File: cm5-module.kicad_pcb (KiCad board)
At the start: 4 copper layers, 100 x 100 mm, 242 parts, among them J1 DIN-41612-connector_090319679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, J10 MicroSD_5033981892, J11 JST_SH_1x4_BM04B-SRSS-TB-LF-SN, J12 USB-C_USB-310F-B-SU, J2 CM5_1-100_3mm-stack, J3 CM5_101-200_3mm-stack, J4 JST_SH_1x3_BM03B-SRSS-TB-LF-SN, J5 Bus_M.2_1-2199230-6, J6 RJ45_HC612601A-M893-A, J7 USB-A_USB-303WSD-BRY, J8 HDMI-A_HDMI-19PIN-043, J9 USB-C_USB-310F-B-SU, Q1 SIS472DN-T1-GE3, Q10 AO3400A, Q2 SIS472DN-T1-GE3, Q3 AO3400A, Q4 SIS472DN-T1-GE3, Q5 AO3400A, Q6 AO3400A, Q7 AO3400A, Q8 AO3401A, Q9 AO3401A, SW1 SW_TL2243, U1 AP22615AWU-7, U10 AP22615AWU-7, U11 AP22615AWU-7, U12 LM74700QDBVRQ1, U13 STM32G431CBU6, U14 STM32G431CBU6, U15 TJA1044GTK_3Z, U16 TJA1044GTK_3Z, U17 FSUSB42UMX, U2 AP22615AWU-7, U3 FT230XQ-R, U4 NTS0102DP, U5 CH334P, U6 LM74700QDBVRQ1, U7 SIC431AED-T1-GE3, U8 LM74700QDBVRQ1, U9 TPS564247DRLR, Y1 Oscillator_32.768kHz_OK2EL89C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, Y2 X322512MSB4SI

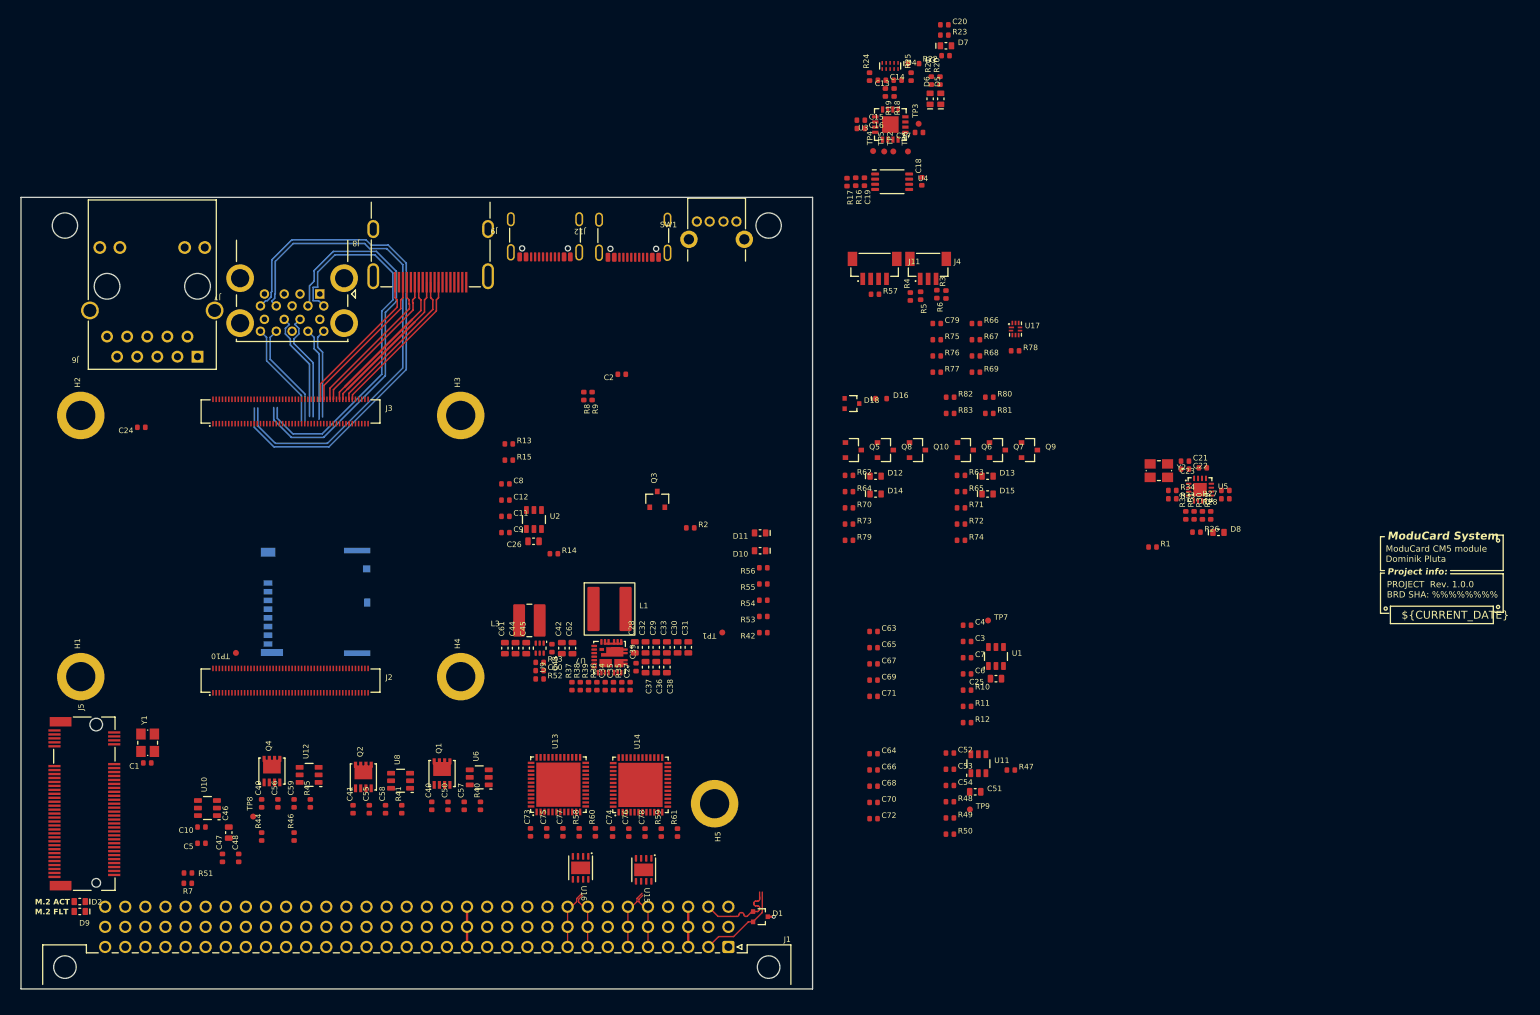
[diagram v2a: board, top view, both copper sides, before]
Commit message: [#3] Fix 3V3 DC-DC converter schematic, change one USB-C to a vertical one, start layout
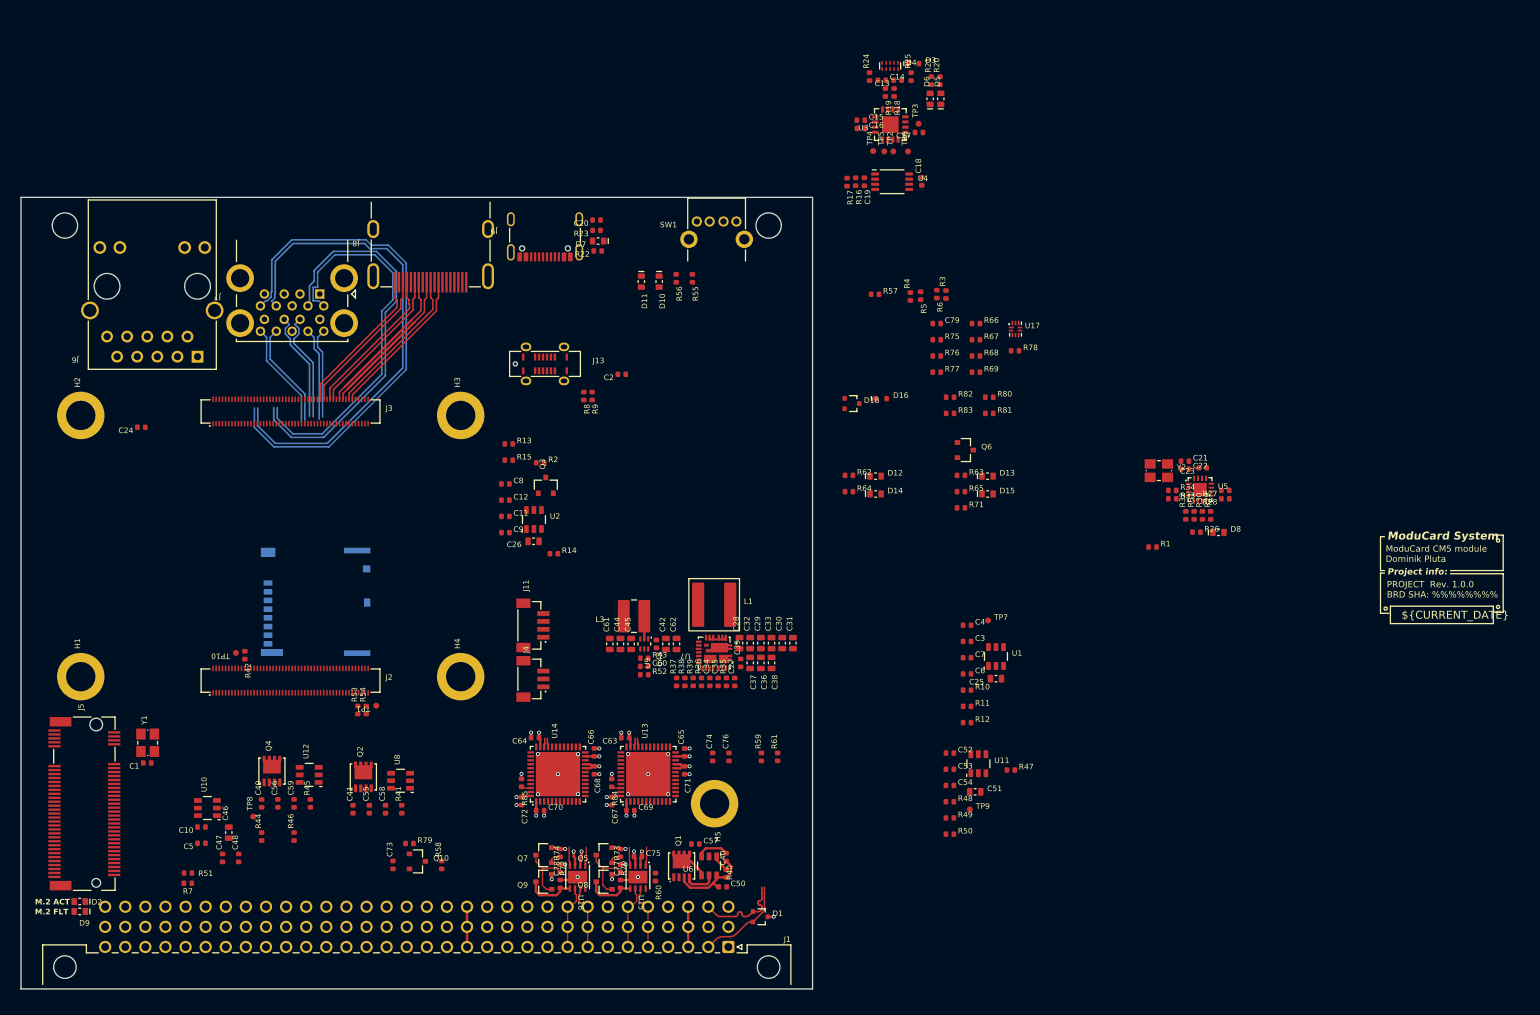
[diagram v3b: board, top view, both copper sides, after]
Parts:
- removed J12: USB-C_USB-310F-B-SU, DW-footprints:USB-C-Receptacle_USB-310-B-SU
- added J13: USB-C_TYPE-C_16PLT-H6.5, DW-footprints:USB-C-Receptacle_TYPE-C_16PLT-H6.5, F.Cu at (106.2, 71.0)
- added R84: R-10k-0402, DW-footprints:R_0402_1005Metric, F.Cu at (114.6, 124.0)
- added R85: R-10k-0402, DW-footprints:R_0402_1005Metric, F.Cu at (103.2, 124.0)
- moved Q9 82.1 mm to (106.0, 136.5), turned to 180 degrees
- moved Q10 81.8 mm to (90.1, 133.9)
- moved Q7 76.8 mm to (106.0, 133.1), turned to 180 degrees
- moved J4 72.6 mm to (104.2, 110.8), turned to 90 degrees
- moved R79 67.5 mm to (89.1, 131.6)
- moved R42 65.6 mm to (68.3, 107.8), turned to -90 degrees
- moved R72 65.5 mm to (108.1, 132.8), turned to -90 degrees
- moved R74 65.4 mm to (108.1, 134.8), turned to 90 degrees
- moved Q8 65.1 mm to (113.7, 136.5), turned to 180 degrees
- moved J11 63.1 mm to (104.2, 104.1), turned to 90 degrees
- moved Q5 60.1 mm to (113.7, 133.1), turned to 180 degrees
- moved R53 52.6 mm to (82.5, 114.8), turned to 90 degrees
- moved R70 52.3 mm to (115.7, 132.8), turned to -90 degrees
- moved R73 52.2 mm to (115.7, 134.8), turned to 90 degrees
- moved R54 52.1 mm to (83.6, 114.8), turned to 90 degrees
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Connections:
- net Net-(U9-FB) renamed /Power/3V3_FB
- C60 pad 2: Net-(U9-SW) -> +3V3
- L3 pad 1: Net-(U9-SW) -> /Power/3V3_SW
- R52 pad 2: Net-(U9-SW) -> +3V3
- U9 pad 2: Net-(U9-SW) -> /Power/3V3_SW
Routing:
- net +3V3: track 0.00 -> 22.9 mm, vias 0 -> 14
- net GND: track 0.76 -> 20.4 mm, vias 1 -> 29
- net +5V_STDBY: track 5.08 -> 15.8 mm
- net Net-(Q7-D): track 0.00 -> 7.97 mm
- net Net-(Q5-D): track 0.00 -> 7.97 mm
- net +5V: track 0.00 -> 7.21 mm, vias 0 -> 2
- net /CAN to USB 2/VIO: track 0.00 -> 6.42 mm
- net /CAN to USB 1/VIO: track 0.00 -> 6.42 mm
- net Net-(Q1-G): track 0.00 -> 4.14 mm
- net /Power/Ideal diode 0/~{DISABLE}: track 0.00 -> 4.08 mm
- net /CAN to USB 1/RXD: track 0.00 -> 3.60 mm
- net /CAN to USB 2/RXD: track 0.00 -> 3.60 mm
- net /Power/3V3_SW: track 0.00 -> 2.86 mm
- net /CAN to USB 2/TXD: track 0.00 -> 2.38 mm
- net /CAN to USB 1/TXD: track 0.00 -> 2.38 mm
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
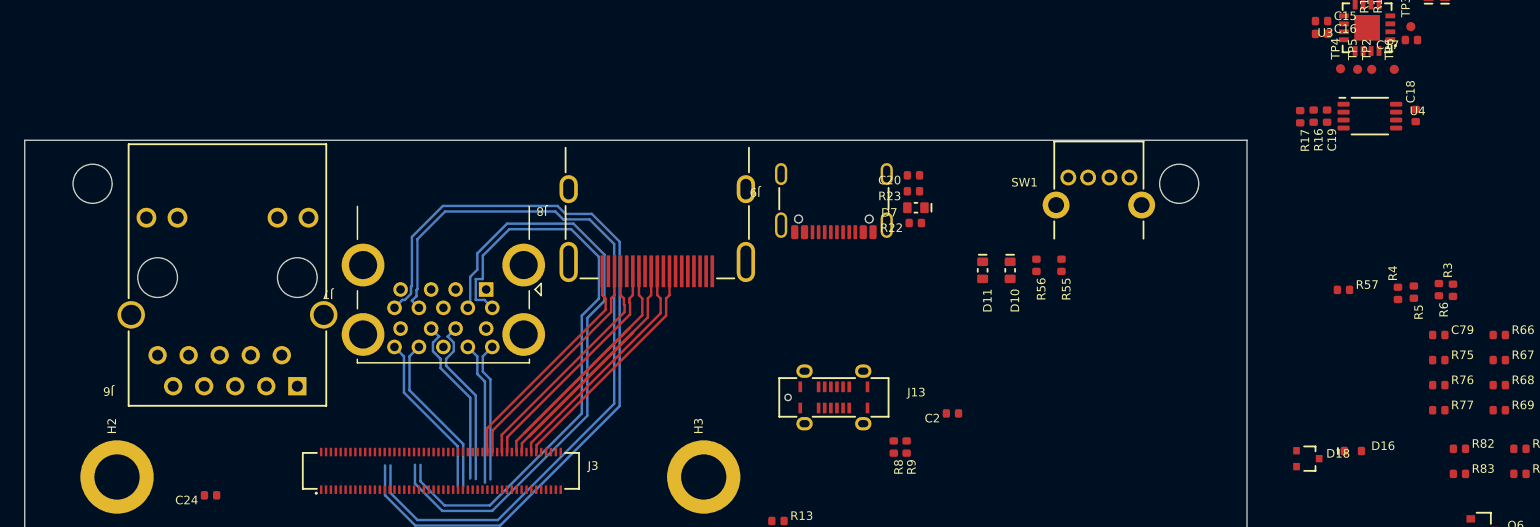
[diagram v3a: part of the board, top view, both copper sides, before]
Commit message: [#3] Adjust front panel mounting holes positioning and rails keepout area
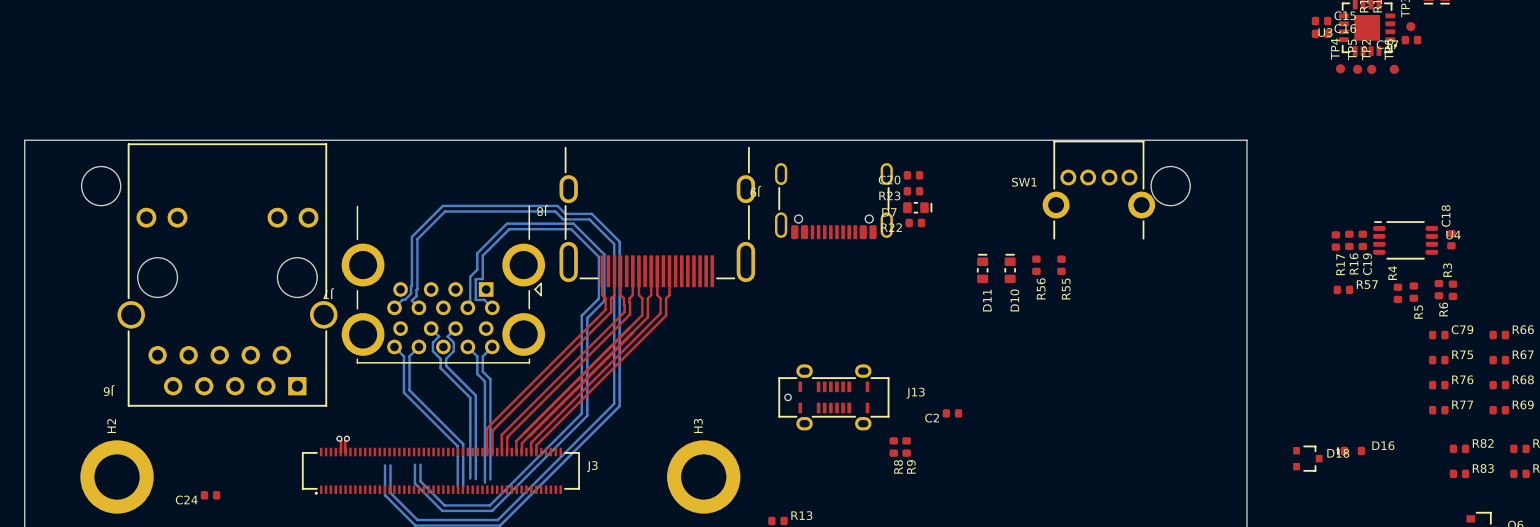
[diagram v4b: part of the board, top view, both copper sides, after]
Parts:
- moved R16 10.6 mm to (148.4, 58.2)
- moved R17 10.6 mm to (147.3, 58.2)
- moved C18 10.6 mm to (156.7, 58.1)
- moved C19 10.6 mm to (149.5, 58.2)
- moved U4 10.6 mm to (153.0, 58.2)
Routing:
- net /CM5/PCIe.REFCLK+: track 0.00 -> 1.16 mm, vias 0 -> 1
- net /CM5/PCIe.REFCLK-: track 0.00 -> 1.16 mm, vias 0 -> 1
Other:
- outline, holes or cut-outs redrawn

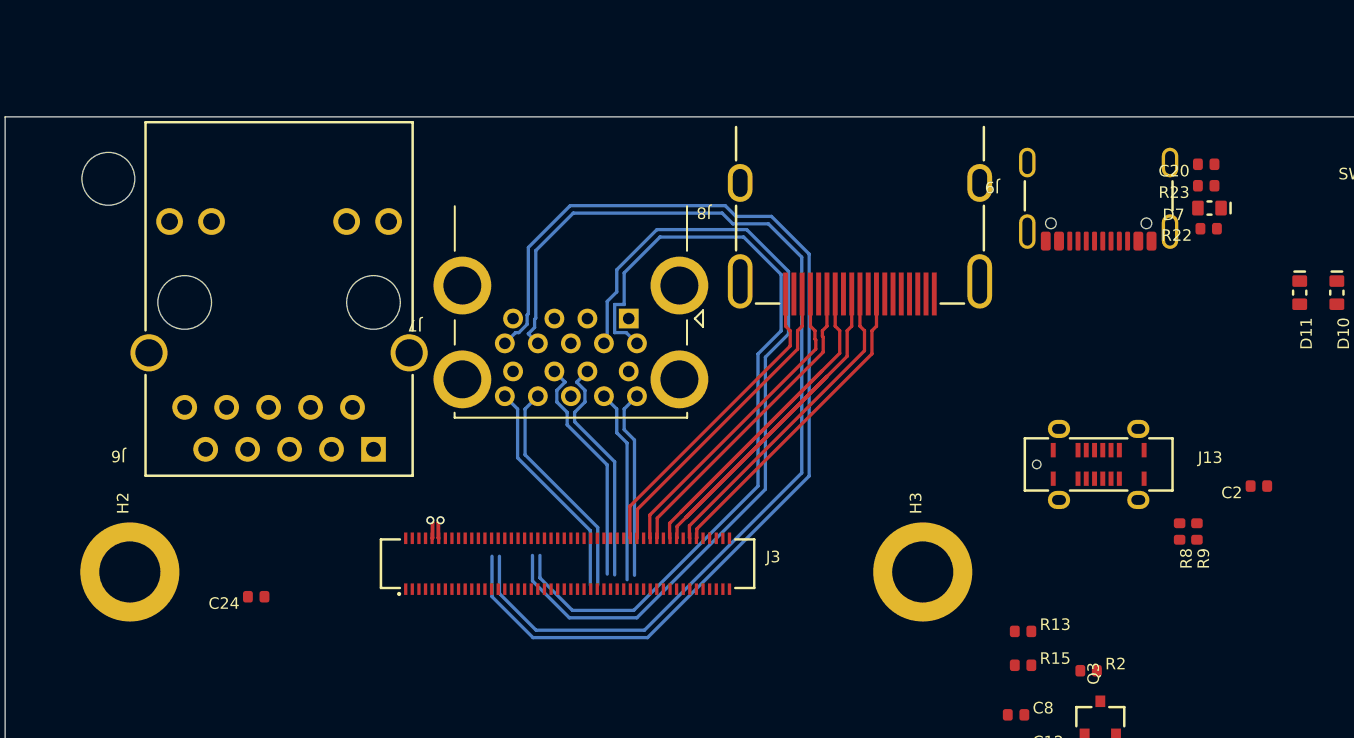
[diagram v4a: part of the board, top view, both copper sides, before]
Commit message: [#3] Position front panel connectors
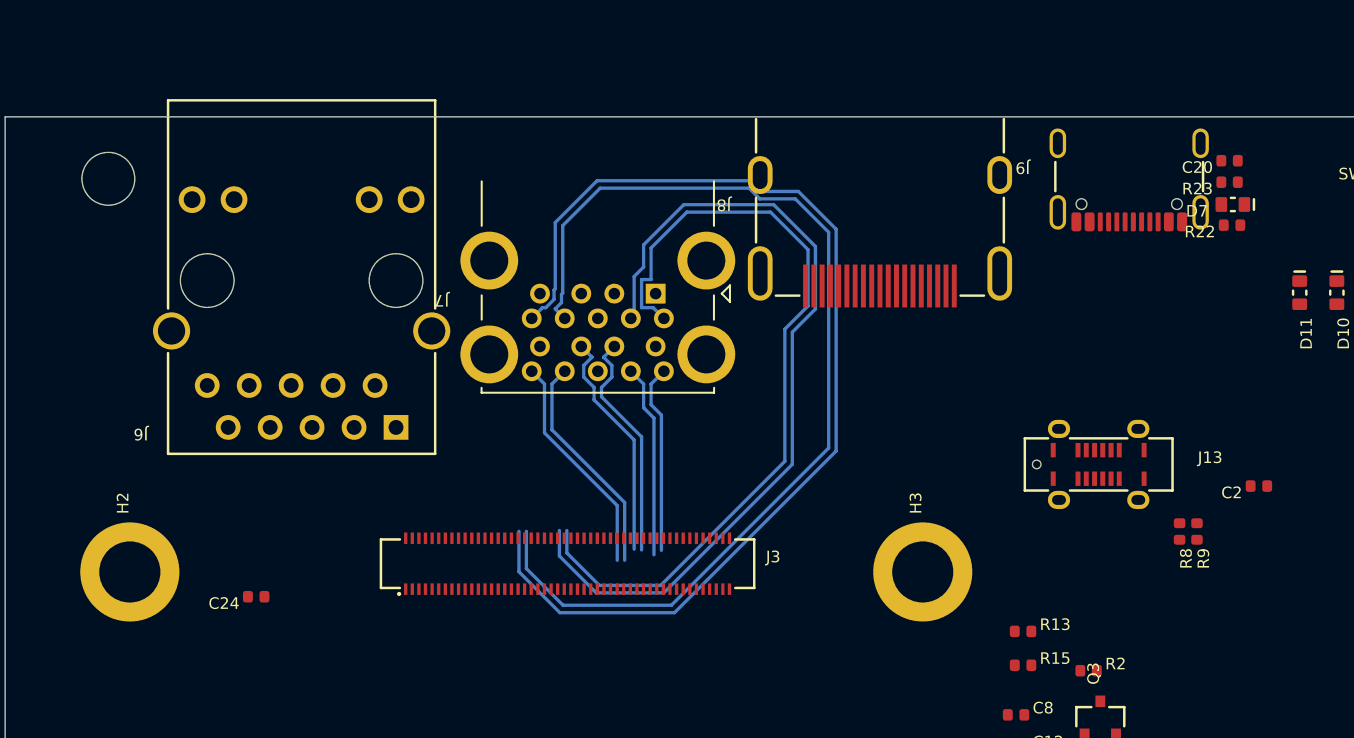
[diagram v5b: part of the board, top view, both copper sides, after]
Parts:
- moved J7 2.22 mm to (79.4, 60.7)
- moved J9 2.19 mm to (108.0, 52.7)
- moved J6 1.90 mm to (63.7, 68.8)
- moved D7 1.43 mm to (114.3, 55.3)
- moved R22 1.43 mm to (114.3, 56.6)
- moved R23 1.43 mm to (114.1, 54.0)
- moved C20 1.43 mm to (114.1, 52.7)
- moved J8 1.30 mm to (93.0, 54.9)
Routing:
- net /CM5/HDMI_0.D0+: track 43.4 -> 0.00 mm
- net /CM5/HDMI_0.D0-: track 43.4 -> 0.00 mm
- net /CM5/HDMI_0.CLK+: track 19.3 -> 0.00 mm
- net /CM5/HDMI_0.CLK-: track 19.3 -> 0.00 mm
- net /CM5/HDMI_0.D1+: track 19.1 -> 0.00 mm
- net /CM5/HDMI_0.D1-: track 19.1 -> 0.00 mm
- net /CM5/HDMI_0.D2+: track 18.9 -> 0.00 mm
- net /CM5/HDMI_0.D2-: track 18.9 -> 0.00 mm
- net /CM5/PCIe.REFCLK+: track 1.16 -> 0.00 mm, vias 1 -> 0
- net /CM5/PCIe.REFCLK-: track 1.16 -> 0.00 mm, vias 1 -> 0
